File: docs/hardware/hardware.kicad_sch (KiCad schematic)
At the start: 2 parts, among them U1 STM32F091RCTx, U2 XC7A35T-CPG236

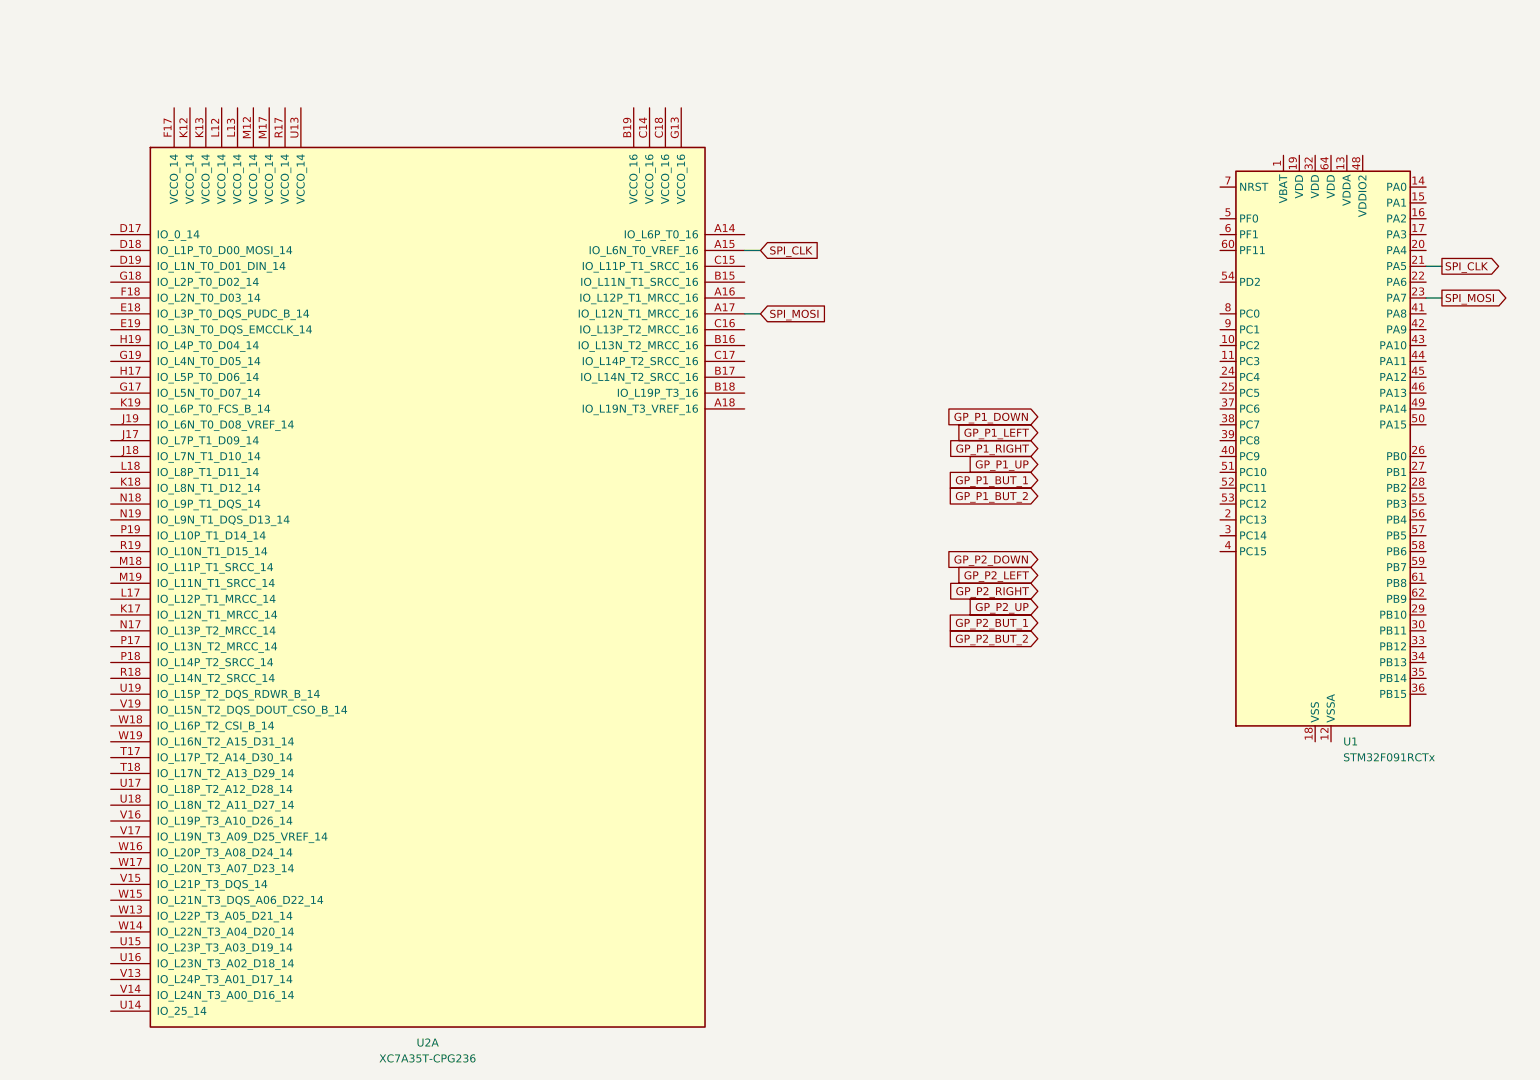
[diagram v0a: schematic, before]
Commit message: update hardware schematics for ppu testing
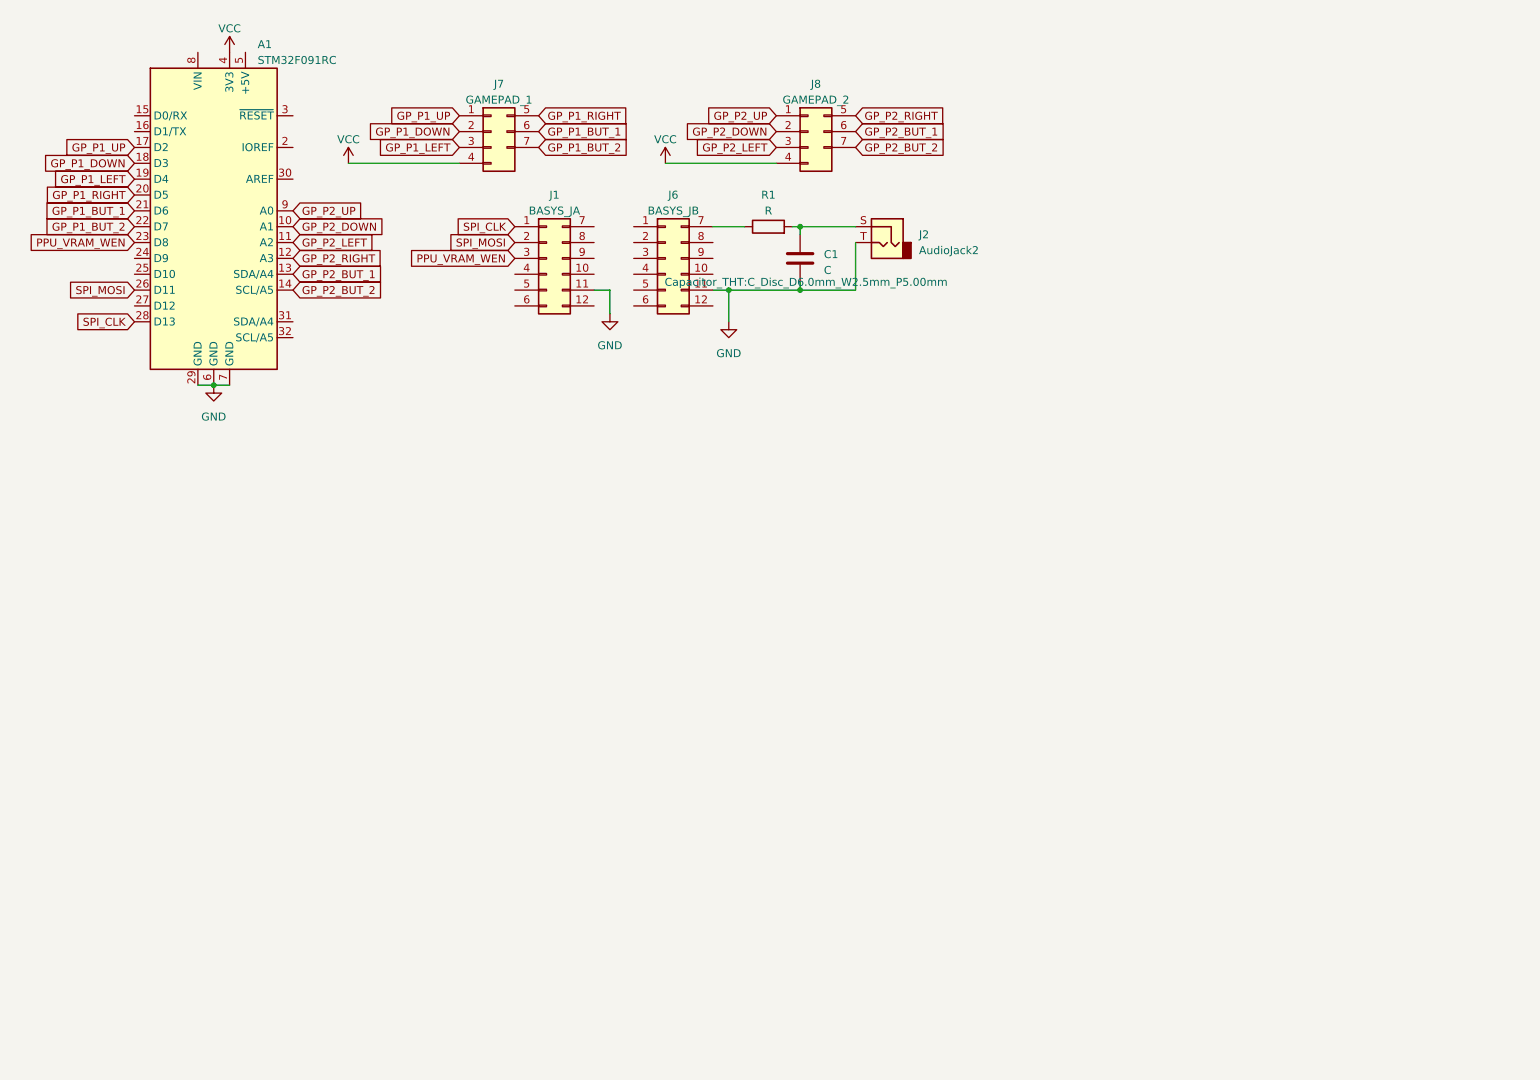
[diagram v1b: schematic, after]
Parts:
- removed U1: STM32F091RCTx, Package_QFP:LQFP-64_10x10mm_P0.5mm, symbol MCU_ST_STM32F0:STM32F091RCTx
- removed U2: XC7A35T-CPG236, symbol FPGA_Xilinx_Artix7:XC7A35T-CPG236
- added A1: STM32F091RC, Module:Arduino_UNO_R3, symbol MCU_Module:Arduino_UNO_R3
- added C1: C, Capacitor_THT:C_Disc_D6.0mm_W2.5mm_P5.00mm, symbol Device:C
- added J1: BASYS_JA, Connector_PinHeader_2.54mm:PinHeader_2x06_P2.54mm_Vertical, symbol Connector_Generic:Conn_02x06_Top_Bottom
- added J2: AudioJack2, Connector_Audio:Jack_3.5mm_CUI_SJ1-3523N_Horizontal, symbol Connector_Audio:AudioJack2
- added J6: BASYS_JB, Connector_PinHeader_2.54mm:PinHeader_2x06_P2.54mm_Vertical, symbol Connector_Generic:Conn_02x06_Top_Bottom
- added J7: GAMEPAD_1, Connector_PinHeader_2.54mm:PinHeader_2x04_P2.54mm_Vertical, symbol Connector_Generic:Conn_02x04_Top_Bottom
- added J8: GAMEPAD_2, Connector_PinHeader_2.54mm:PinHeader_2x04_P2.54mm_Vertical, symbol Connector_Generic:Conn_02x04_Top_Bottom
- added R1: R, Resistor_THT:R_Axial_DIN0207_L6.3mm_D2.5mm_P7.62mm_Horizontal, symbol Device:R
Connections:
- net GP_P1_BUT_1: now also A1.21 (D6), J7.6 (PRIMARY)
- net GP_P1_BUT_2: now also A1.22 (D7), J7.7 (SECONDARY)
- net GP_P1_DOWN: now also A1.18 (D3), J7.2 (DOWN)
- net GP_P1_LEFT: now also A1.19 (D4), J7.3 (LEFT)
- net GP_P1_RIGHT: now also A1.20 (D5), J7.5 (RIGHT)
- net GP_P1_UP: now also A1.17 (D2), J7.1 (UP)
- net GP_P2_BUT_1: now also A1.13 (SDA/A4), J8.6 (PRIMARY)
- net GP_P2_BUT_2: now also A1.14 (SCL/A5), J8.7 (SECONDARY)
- net GP_P2_DOWN: now also A1.10 (A1), J8.2 (DOWN)
- net GP_P2_LEFT: now also A1.11 (A2), J8.3 (LEFT)
- net GP_P2_RIGHT: now also A1.12 (A3), J8.5 (RIGHT)
- net GP_P2_UP: now also A1.9 (A0), J8.1 (UP)
- net SPI_CLK: now also A1.28 (D13), J1.1 (Pin_1)
- net SPI_MOSI: now also A1.26 (D11), J1.2 (Pin_2)
- new net: C1.1, J2.S, R1.2
- new net: J6.7 (Pin_7), R1.1
- new net GND: A1.29 (GND), A1.6 (GND), A1.7 (GND), C1.2, J1.11 (Pin_11), J2.T, J6.11 (Pin_11)
- new net PPU_VRAM_WEN: A1.23 (D8), J1.3 (Pin_3)
- new net VCC: A1.4 (3V3), J7.4 (VCC), J8.4 (VCC)

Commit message: WIP ppu testing
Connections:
- net GND: now also J1.5 (Pin_5), J6.5 (Pin_5)
- net PPU_VRAM_WEN: now also J1.1 (Pin_1); no longer J1.3 (Pin_3)
- net SPI_CLK: now also J1.3 (Pin_3); no longer J1.1 (Pin_1)
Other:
- moved on the sheet: C1, J2, J6, R1

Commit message: finalize hardware
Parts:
- added J3: GAMEPAD, Connector_PinHeader_2.54mm:PinHeader_2x04_P2.54mm_Vertical, symbol Connector_Generic:Conn_02x04_Top_Bottom
- added SW1: LEFT, Button_Switch_THT:SW_PUSH_6mm, symbol Switch:SW_Push_SPDT
- added SW2: UP, Button_Switch_THT:SW_PUSH_6mm, symbol Switch:SW_Push_SPDT
- added SW3: RIGHT, Button_Switch_THT:SW_PUSH_6mm, symbol Switch:SW_Push_SPDT
- added SW4: PRIMARY, Button_Switch_THT:SW_PUSH_6mm, symbol Switch:SW_Push_SPDT
- added SW5: SECONDARY, Button_Switch_THT:SW_PUSH_6mm, symbol Switch:SW_Push_SPDT
- added SW6: DOWN, Button_Switch_THT:SW_PUSH_6mm, symbol Switch:SW_Push_SPDT
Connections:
- net GP_P1_BUT_1: now also A1.19 (D4), J7.5 (RIGHT); no longer A1.21 (D6), J7.6 (PRIMARY)
- net GP_P1_BUT_2: now also A1.18 (D3), J7.6 (PRIMARY); no longer A1.22 (D7), J7.7 (SECONDARY)
- net GP_P1_DOWN: now also A1.17 (D2), J7.7 (SECONDARY); no longer A1.18 (D3), J7.2 (DOWN)
- net GP_P1_LEFT: now also A1.20 (D5), J7.1 (UP); no longer A1.19 (D4), J7.3 (LEFT)
- net GP_P1_RIGHT: now also A1.22 (D7), J7.3 (LEFT); no longer A1.20 (D5), J7.5 (RIGHT)
- net GP_P1_UP: now also A1.21 (D6), J7.2 (DOWN); no longer A1.17 (D2), J7.1 (UP)
- net GP_P2_BUT_1: now also A1.11 (A2), J8.5 (RIGHT); no longer A1.13 (SDA/A4), J8.6 (PRIMARY)
- net GP_P2_BUT_2: now also A1.10 (A1), J8.6 (PRIMARY); no longer A1.14 (SCL/A5), J8.7 (SECONDARY)
- net GP_P2_DOWN: now also A1.9 (A0), J8.7 (SECONDARY); no longer A1.10 (A1), J8.2 (DOWN)
- net GP_P2_LEFT: now also A1.12 (A3), J8.1 (UP); no longer A1.11 (A2), J8.3 (LEFT)
- net GP_P2_RIGHT: now also A1.14 (SCL/A5), J8.3 (LEFT); no longer A1.12 (A3), J8.5 (RIGHT)
- net GP_P2_UP: now also A1.13 (SDA/A4), J8.2 (DOWN); no longer A1.9 (A0), J8.1 (UP)
- new net: J3.5 (RIGHT), SW4.1 (A)
- new net: J3.4 (VCC), SW1.2 (B), SW2.2 (B), SW3.2 (B), SW4.2 (B), SW5.2 (B), SW6.2 (B)
- new net: J3.2 (DOWN), SW2.1 (A)
- new net: J3.1 (UP), SW1.1 (A)
- new net: J3.3 (LEFT), SW3.1 (A)
- new net: J3.6 (PRIMARY), SW5.1 (A)
- new net: J3.7 (SECONDARY), SW6.1 (A)

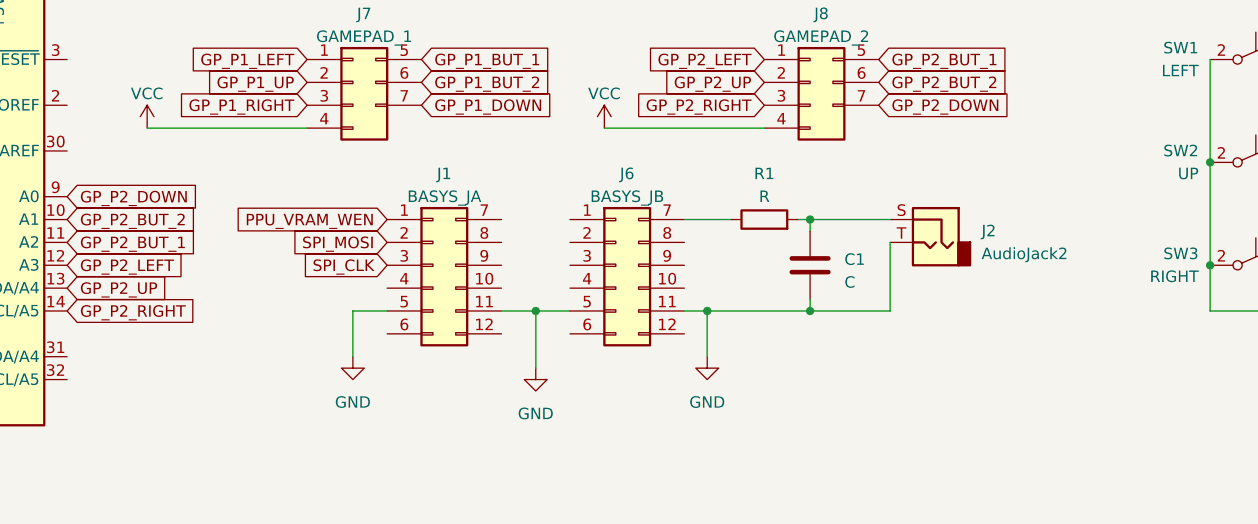
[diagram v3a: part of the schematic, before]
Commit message: add power source toggle switch to hardware schematics
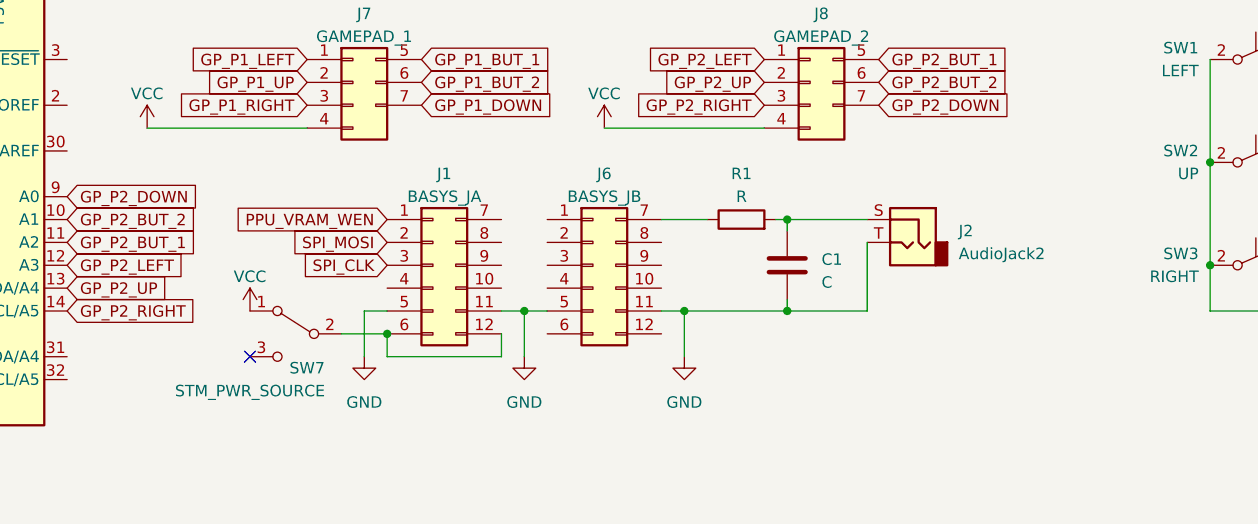
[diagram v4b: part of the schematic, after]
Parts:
- added SW7: STM_PWR_SOURCE, Button_Switch_THT:SW_Slide_1P2T_CK_OS102011MS2Q, symbol Switch:SW_SPDT
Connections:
- net VCC: now also SW7.1 (A)
- net at J1.12 (Pin_12): now also J1.6 (Pin_6), SW7.2 (B)
- no-connect marks 0 -> 1
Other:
- moved on the sheet: C1, J2, J6, R1

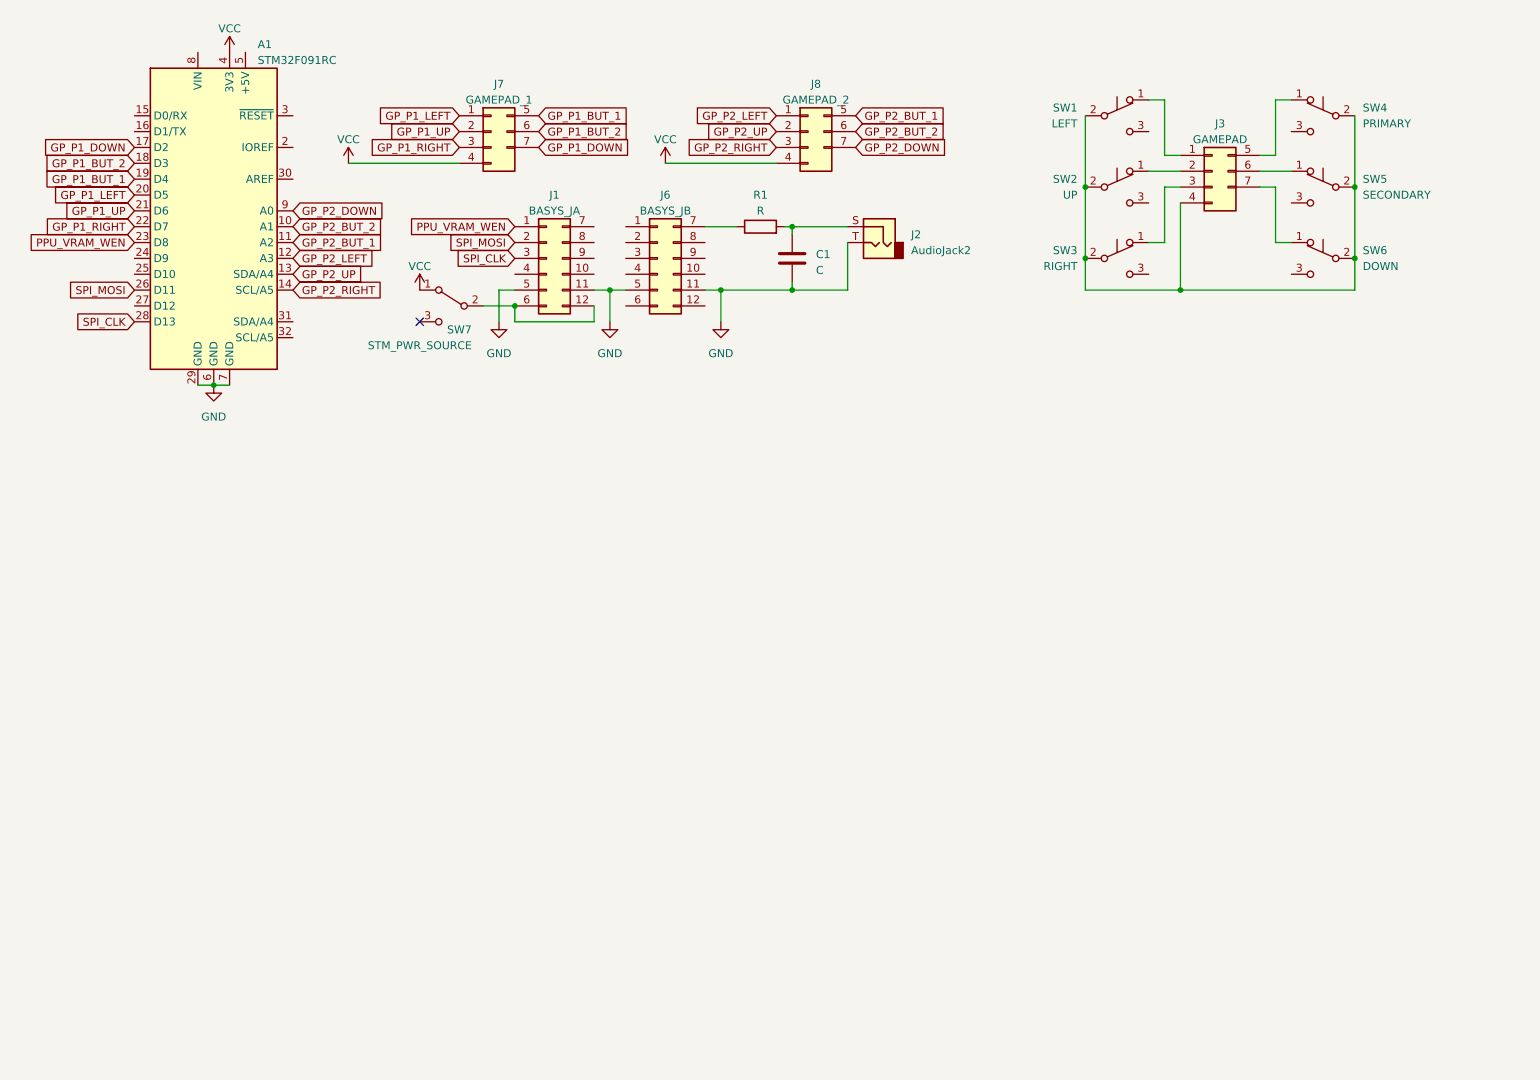
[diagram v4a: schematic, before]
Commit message: connect remaining ppu lines to stm
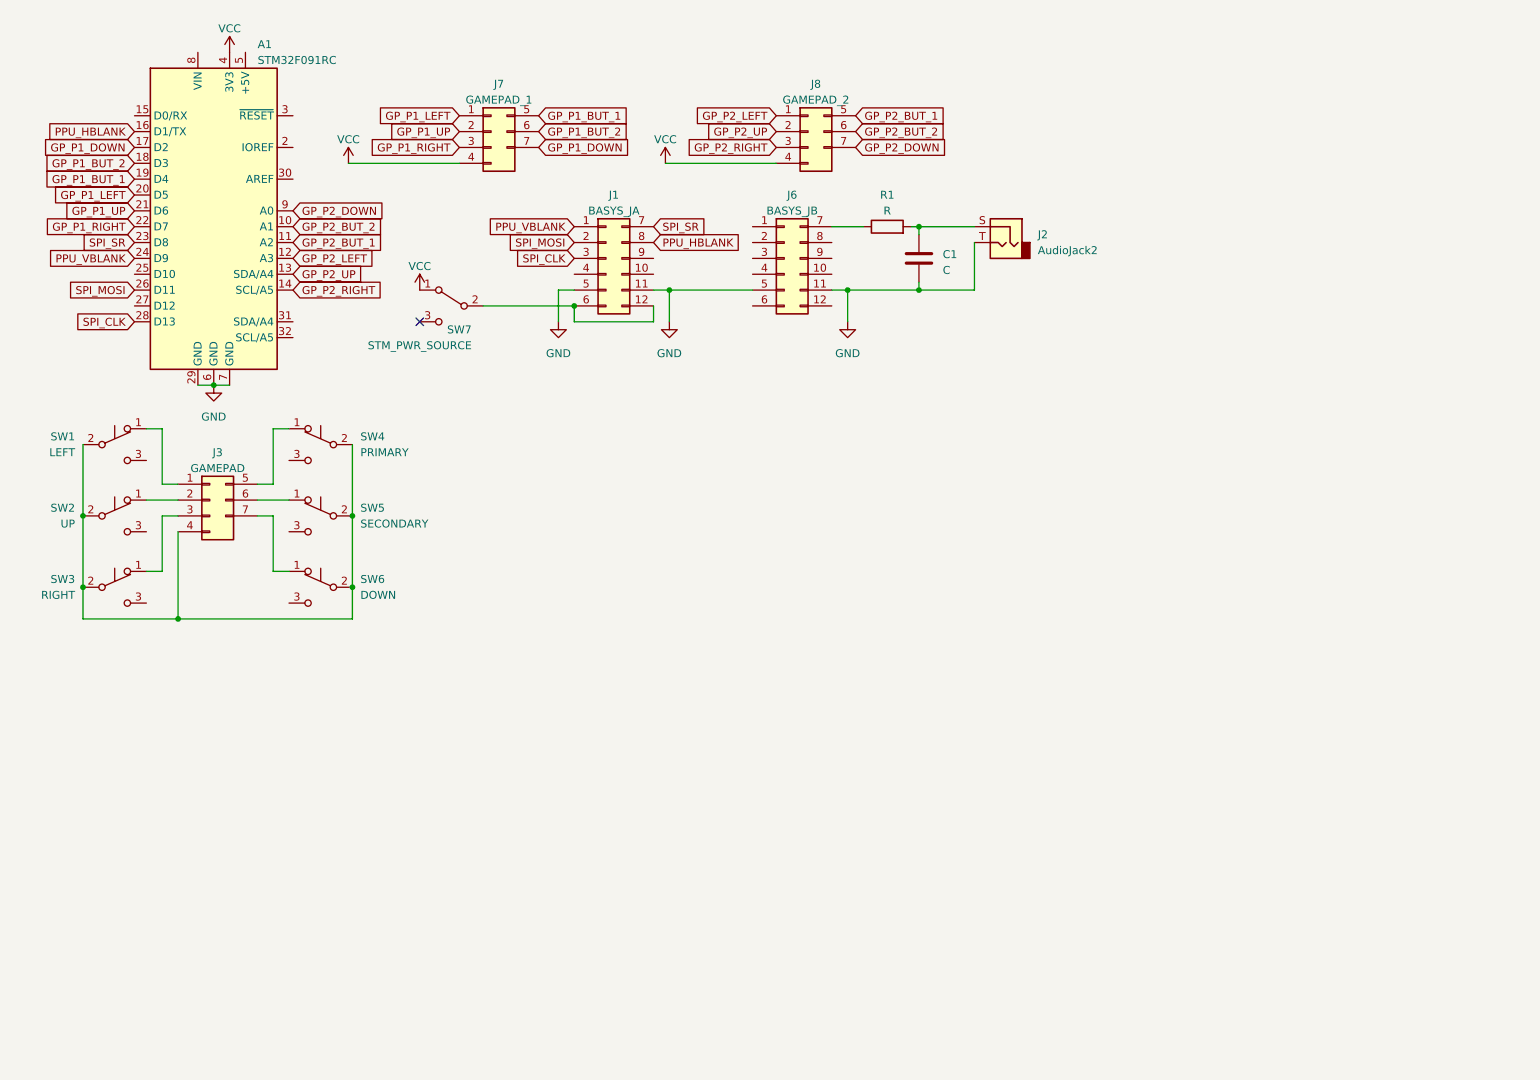
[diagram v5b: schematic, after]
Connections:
- net SPI_SR: now reaches J1.7 (Pin_7)
- net SPI_SR: now also A1.23 (D8)
- net PPU_HBLANK: now reaches J1.8 (Pin_8)
- net PPU_HBLANK: now also A1.16 (D1/TX)
- net PPU_VBLANK: now reaches A1.24 (D9)
- net PPU_VBLANK: now also J1.1 (Pin_1)
- removed net PPU_VRAM_WEN: A1.23 (D8), J1.1 (Pin_1)
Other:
- moved on the sheet: C1, J1, J2, J3, J6, R1, SW1, SW2, SW3, SW4, SW5, SW6

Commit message: final I/O edits
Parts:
- added R2: R, Resistor_THT:R_Axial_DIN0207_L6.3mm_D2.5mm_P7.62mm_Horizontal, symbol Device:R
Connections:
- net GND: now also R2.1
- net GP_P1_BUT_1: now also A1.17 (D2); no longer A1.19 (D4)
- net GP_P1_BUT_2: now also A1.16 (D1/TX); no longer A1.18 (D3)
- net GP_P1_DOWN: now also A1.15 (D0/RX); no longer A1.17 (D2)
- net GP_P1_LEFT: now also A1.18 (D3); no longer A1.20 (D5)
- net GP_P1_RIGHT: now also A1.20 (D5); no longer A1.22 (D7)
- net GP_P1_UP: now also A1.19 (D4); no longer A1.21 (D6)
- net PPU_HBLANK: now also A1.22 (D7); no longer A1.16 (D1/TX)
- net SPI_SR: now also R2.2
- net unused: now reaches J1.9 (Pin_9)
- net unused: now also A1.21 (D6)
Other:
- moved on the sheet: C1, J1, J2, J6, J7, J8, R1, SW7
